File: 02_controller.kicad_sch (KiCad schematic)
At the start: 55 parts, among them J5 ISP 2x3, SW1 DIP bit 0, SW10 DIP bit 9, SW11 DIP bit 10, SW12 DIP bit 11, SW13 APPLY momentary NO, SW2 DIP bit 1, SW3 DIP bit 2, SW4 DIP bit 3, SW5 DIP bit 4, SW6 DIP bit 5, SW7 DIP bit 6, SW8 DIP bit 7, SW9 DIP bit 8, U2 1887VE7T / 4203.64-2, U6 SN74LVC125APWR, U7 SN74AHCT1G125DBVR

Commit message: Rev D schematic: ГОСТ symbols and designators in KiCad, footprints
- Three sheets regenerated by tools/dds_build.py (DDS A2, controller A3,
  power A2) with ГОСТ 2.743 symbols, ГОСТ 2.710 designators (D1.1, XW1, S2)
  and a ГОСТ 2.104 drawing sheet (lib/GOST_E3.kicad_wks).
- Connectivity identical to rev C (tools/netcompare.py with
  verification/refmap_revC_to_revD.json): 160 components, 139 nets; the 12
  single DIP switches are grouped into DIP-8 + DIP-4 packages.
- ERC: 0 errors, 0 warnings. Footprints assigned; project library lib/
  (1508PL8T LQFP-100, 1887VE7T CQFP-64 4203.64-2 preliminary, GK361-TK-02
  placeholder - not confirmed, DNP).
- Old rev C PDF replaced by output/pdf/DDS_47_51_sch.pdf.

Co-Authored-By: Claude Opus 5.5 <noreply@anthropic.com>
Claude-Session: https://claude.ai/code/session_018GorfTmWz53k1K9rRxWMAW
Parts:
- removed C39, C40, C44, C45, C46: 100n, symbol Local:C
- removed C41: 100n / U2.21, symbol Local:C
- removed C42: 100n / U2.52, symbol Local:C
- removed C43: 100n / U2.64, symbol Local:C
- removed J5: ISP 2x3, symbol Local:J6
- removed R36, R37, R38, R39, R40, R41, R42, R43, R44, R45, R46, R47, R48, R49, R50, R57, R58, R59, R60, R61, R62, R63, R64, R65: 10k, symbol Local:R
- removed R51, R52, R53, R54: 33R, symbol Local:R
- removed R55: 1k, symbol Local:R
- removed R56: 100k, symbol Local:R
- removed SW1: DIP bit 0, symbol Local:SW_SPST
- removed SW10: DIP bit 9, symbol Local:SW_SPST
- removed SW11: DIP bit 10, symbol Local:SW_SPST
- removed SW12: DIP bit 11, symbol Local:SW_SPST
- removed SW13: APPLY momentary NO, symbol Local:SW_SPST
- removed SW2: DIP bit 1, symbol Local:SW_SPST
- removed SW3: DIP bit 2, symbol Local:SW_SPST
- removed SW4: DIP bit 3, symbol Local:SW_SPST
- removed SW5: DIP bit 4, symbol Local:SW_SPST
- removed SW6: DIP bit 5, symbol Local:SW_SPST
- removed SW7: DIP bit 6, symbol Local:SW_SPST
- removed SW8: DIP bit 7, symbol Local:SW_SPST
- removed SW9: DIP bit 8, symbol Local:SW_SPST
- removed U2: 1887VE7T / 4203.64-2, symbol Local:1887VE7T
- removed U6: SN74LVC125APWR, symbol Local:LVC125
- removed U7: SN74AHCT1G125DBVR, symbol Local:AHCT1G125
- added C38, C39, C40, C41, C42, C43, C44, C45: 100n, Capacitor_SMD:C_0603_1608Metric, symbol DDS:C
- added D2: 1887ВЕ7Т, DDS:CQFP-64_4203.64-2_14x14mm_P0.8mm_1887VE7T, symbol DDS:1887VE7T
- added D3: SN74LVC125APWR, Package_SO:TSSOP-14_4.4x5mm_P0.65mm, symbol DDS:SN74LVC125A
- added D4: SN74AHCT1G125DBVR, Package_TO_SOT_SMD:SOT-23-5, symbol DDS:SN74AHCT1G125
- added R48, R49, R50, R51, R52, R53, R54, R55, R56, R57, R58, R59, R60, R61, R62, R63, R64, R65, R66, R67, R72, R73, R74, R75: 10k, Resistor_SMD:R_0603_1608Metric, symbol DDS:R
- added R68, R69, R70, R71: 33R, Resistor_SMD:R_0603_1608Metric, symbol DDS:R
- added R76: 1k, Resistor_SMD:R_0603_1608Metric, symbol DDS:R
- added R77: 100k, Resistor_SMD:R_0603_1608Metric, symbol DDS:R
- added S2: DIP-8, Button_Switch_THT:SW_DIP_SPSTx08_Slide_9.78x22.5mm_W7.62mm_P2.54mm, symbol DDS:S_DIP_x08
- added S3: DIP-4, Button_Switch_THT:SW_DIP_SPSTx04_Slide_9.78x12.34mm_W7.62mm_P2.54mm, symbol DDS:S_DIP_x04
- added S4: 6x6, Button_Switch_THT:SW_PUSH_6mm, symbol DDS:SB
- added X1: PLD-6, Connector_PinHeader_2.54mm:PinHeader_2x03_P2.54mm_Vertical, symbol DDS:X_6
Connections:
- net +3V3: now also C44.1, D3.14 (VCC), R67.1, R74.1
- net +5V: now also C41.1, C42.1, C43.1, C45.1, D2.21 (VCC), D2.52 (VCC), D2.64 (AVCC), D4.5 (VCC), R48.1, R49.1, R50.1, R51.1, R52.1, R53.1, R54.1, R55.1, R56.1, R57.1, R58.1, R59.1, R60.1, R61.1, R62.1, R65.1, X1.2
- net APPLYn: now also C38.1, D2.40 (PC5), R60.2, S4.1
- net BUF_OEn: now also D2.15 (PB5), D3.1 (EN), D3.10 (EN), D3.13 (EN), D3.4 (EN), R67.2
- net CS_BUF: now also D3.8, R70.1
- net DDS_PGOOD: now also D2.39 (PC4)
- net DDS_RSTn: now also R71.2, R75.1
- net DDS_SCK: now also R68.2, R72.1
- net DDS_SCSn: now also R70.2, R74.2
- net DDS_SDI: now also R69.2, R73.1
- net DDS_SDO: now also R76.1
- net DIP0: now also D2.51 (PA0), R48.2, S2.1
- net DIP1: now also D2.50 (PA1), R49.2, S2.2
- net DIP10: now also D2.37 (PC2), R58.2, S3.3
- net DIP11: now also D2.38 (PC3), R59.2, S3.4
- net DIP2: now also D2.49 (PA2), R50.2, S2.3
- net DIP3: now also D2.48 (PA3), R51.2, S2.4
- net DIP4: now also D2.47 (PA4), R52.2, S2.5
- net DIP5: now also D2.46 (PA5), R53.2, S2.6
- net DIP6: now also D2.45 (PA6), R54.2, S2.7
- net DIP7: now also D2.44 (PA7), R55.2, S2.8
- net DIP8: now also D2.35 (PC0), R56.2, S3.1
- net DIP9: now also D2.36 (PC1), R57.2, S3.2
- net GND: now also C38.2, C39.2, C40.2, C41.2, C42.2, C43.2, C44.2, C45.2, D2.22 (GND), D2.53 (GND), D2.63 (AGND), D3.7 (GND), D4.1 (EN), D4.3 (GND), R63.2, R64.2, R66.2, R72.2, R73.2, R75.2, R77.2, S2.10, S2.11, S2.12, S2.13, S2.14, S2.15, S2.16, S2.9, S3.5, S3.6, S3.7, S3.8, S4.2, X1.6
- net ISP_PDI: now also D2.2 (PE0), X1.4
- net ISP_PDO: now also D2.3 (PE1), X1.1
- net MCU_CS: now also D2.10 (PB0), D3.9, R65.2
- net MCU_DDS_RESET: now also D2.14 (PB4), D3.12, R66.1
- net MCU_MISO: now also D2.13 (PB3), D4.4
- net MCU_MOSI: now also D2.12 (PB2), D3.5, R64.1
- net MCU_RESETn: now also C39.1, D2.20 (RESET), R61.2, X1.5
- net MCU_SCK: now also D2.11 (PB1), D3.2, R63.1, X1.3
- net MOSI_BUF: now also D3.6, R69.1
- net RST_BUF: now also D3.11, R71.1
- net SCK_BUF: now also D3.3, R68.1
- net SDO_BUF: now also D4.2, R76.2, R77.1
- new net: D2.1 (PEN), R62.2
- new net: C40.1, D2.62 (AREF)
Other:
- note added: "D3 выключен при старте (R67); PB5 D2 — только «0» или вход"
- note added: "S2 — DIP-8 (биты 0–7), S3 — DIP-4 (биты 8–11); подтяжки R48–R59 10 кОм"
- note added: "SDO 3,3 В → 5 В через D4 (ТТЛ-входы)"
- note added: "ВКЛ (замкнут) = 1 (программная инверсия); N = 0…4000, 4001…4095 отвергаются"
- note added: "Код частоты N = Σ бит·2^i; f = 47 000 000 + 1000·N Гц"
- note added: "Согласование уровней SPI 5 В → 3,3 В"
- note removed: "02 CONTROLLER / 1887VE7T / +5 V"
- note removed: "12-bit selector / ON = 1 / N = 0..4000"
- note removed: "SPI level translation / start at 100 kHz"
- note removed: "f = 47,000,000 + 1,000*N Hz. Reject N > 4000. Debounce APPLY. Internal RC 8 MHz; ISP uses PE0/PE1. See design_notes.md for startup sequence."
- title: Controller, frequency selector and SPI -> Синтезатор частоты 47–51 МГц

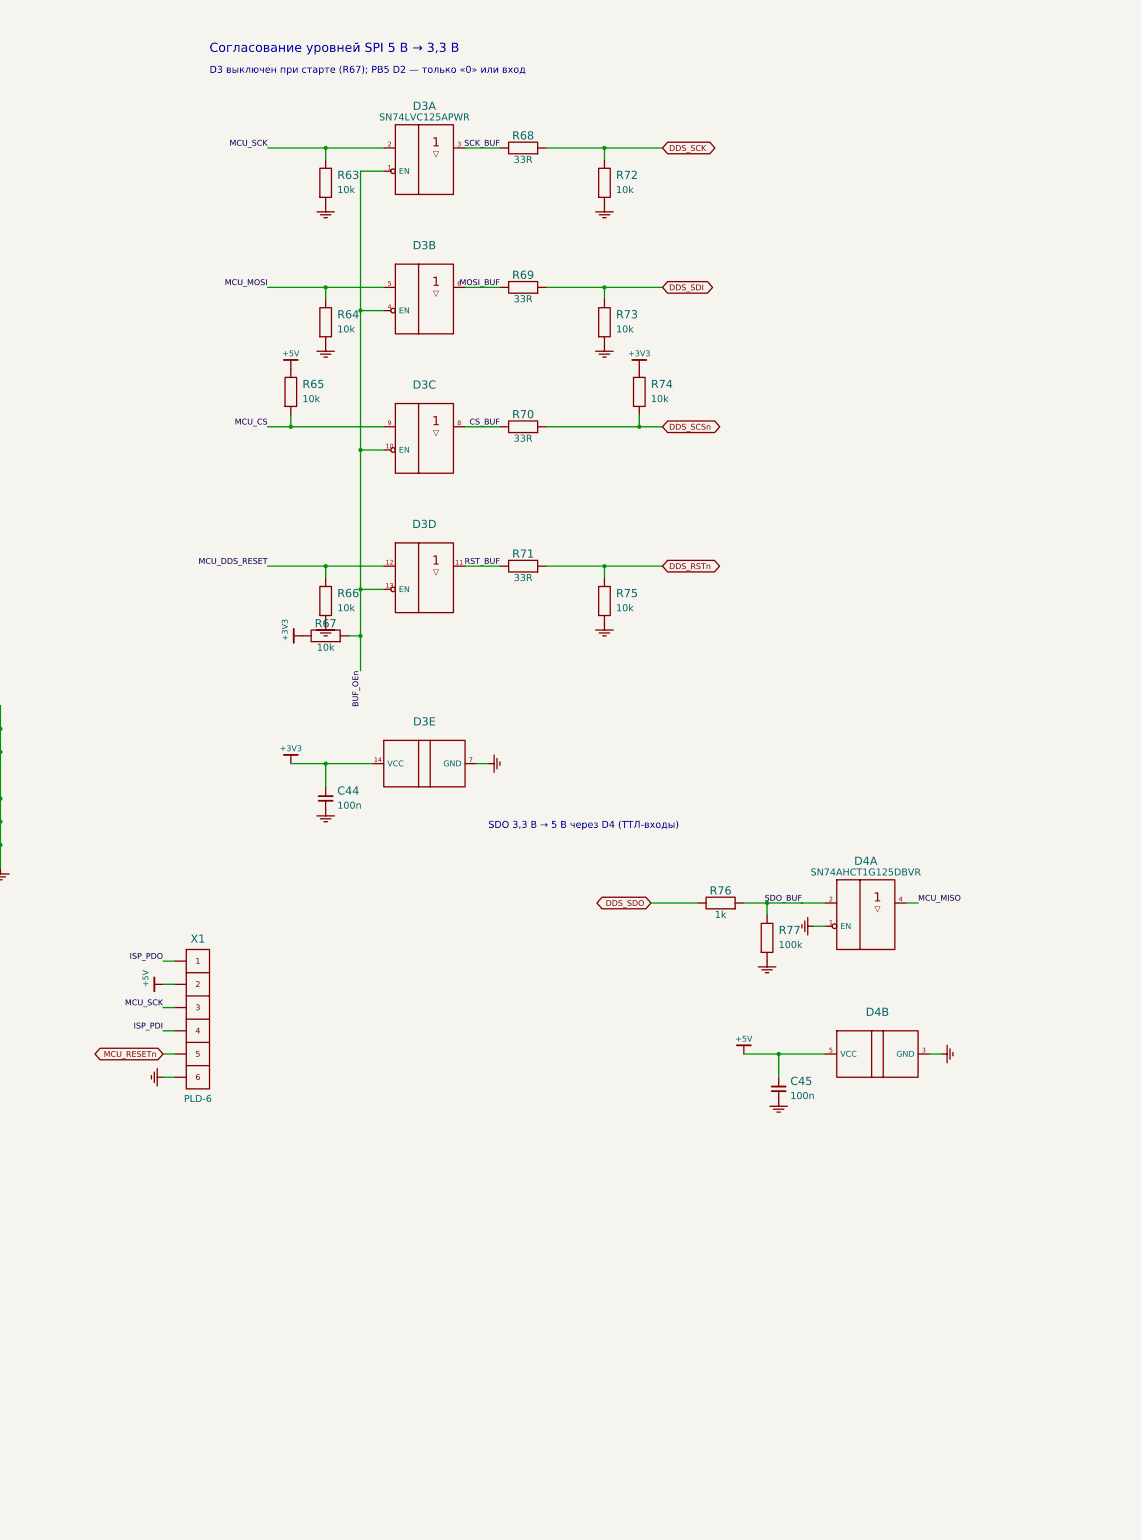
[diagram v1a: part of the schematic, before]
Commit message: Rev E: domestic regulators and logic (1393ЕУ014 + LDO, 1564АП3У2, 1594ТЛ2Т)
Power: TPS62161/2/3 replaced by a two-stage "DC/DC + LDO" scheme:
- D5 1393ЕУ014 +15 V -> +5,02 V (maker's spec v2.1 pinout; FB 40,2k/10k,
  CL 909 Ohm, soft start 100k/0,22u, EXT compensation 10k + 0,1u,
  L8 56 uH, VD2 2Д2990А, 22 uF + 100 uF tantalum output); PG -> MCU reset
- D6 1158ЕН3.3ВХ +5 V -> +3,3 V, D7 1325ЕН1.8У +5 V -> +1,8 V with a
  +5V copper heat spreader on F.Cu/B.Cu (up to 1,3 W)
- 1272ПН3Т is not used (customer decision)

SPI level shifting: SN74LVC125A -> 1564АП3У2 from +3,3 V with 1 kOhm series
resistors on all five 5 V inputs including 1OE#; SN74AHCT1G125 -> two
inverters of 1594ТЛ2Т from +5 V.

Connectivity changes in tools/eco.py; verified against the intended rev E
netlist and, for untouched parts, against rev C. ERC 0; board re-placed and
routed, DRC with schematic parity 0. Land patterns of all new domestic parts
are PLACEHOLDERS (not for fabrication). tools/pro_merge.py restores the
schematic settings that pcbnew drops from the .kicad_pro.

Co-Authored-By: Claude Opus 5.5 <noreply@anthropic.com>
Claude-Session: https://claude.ai/code/session_018GorfTmWz53k1K9rRxWMAW
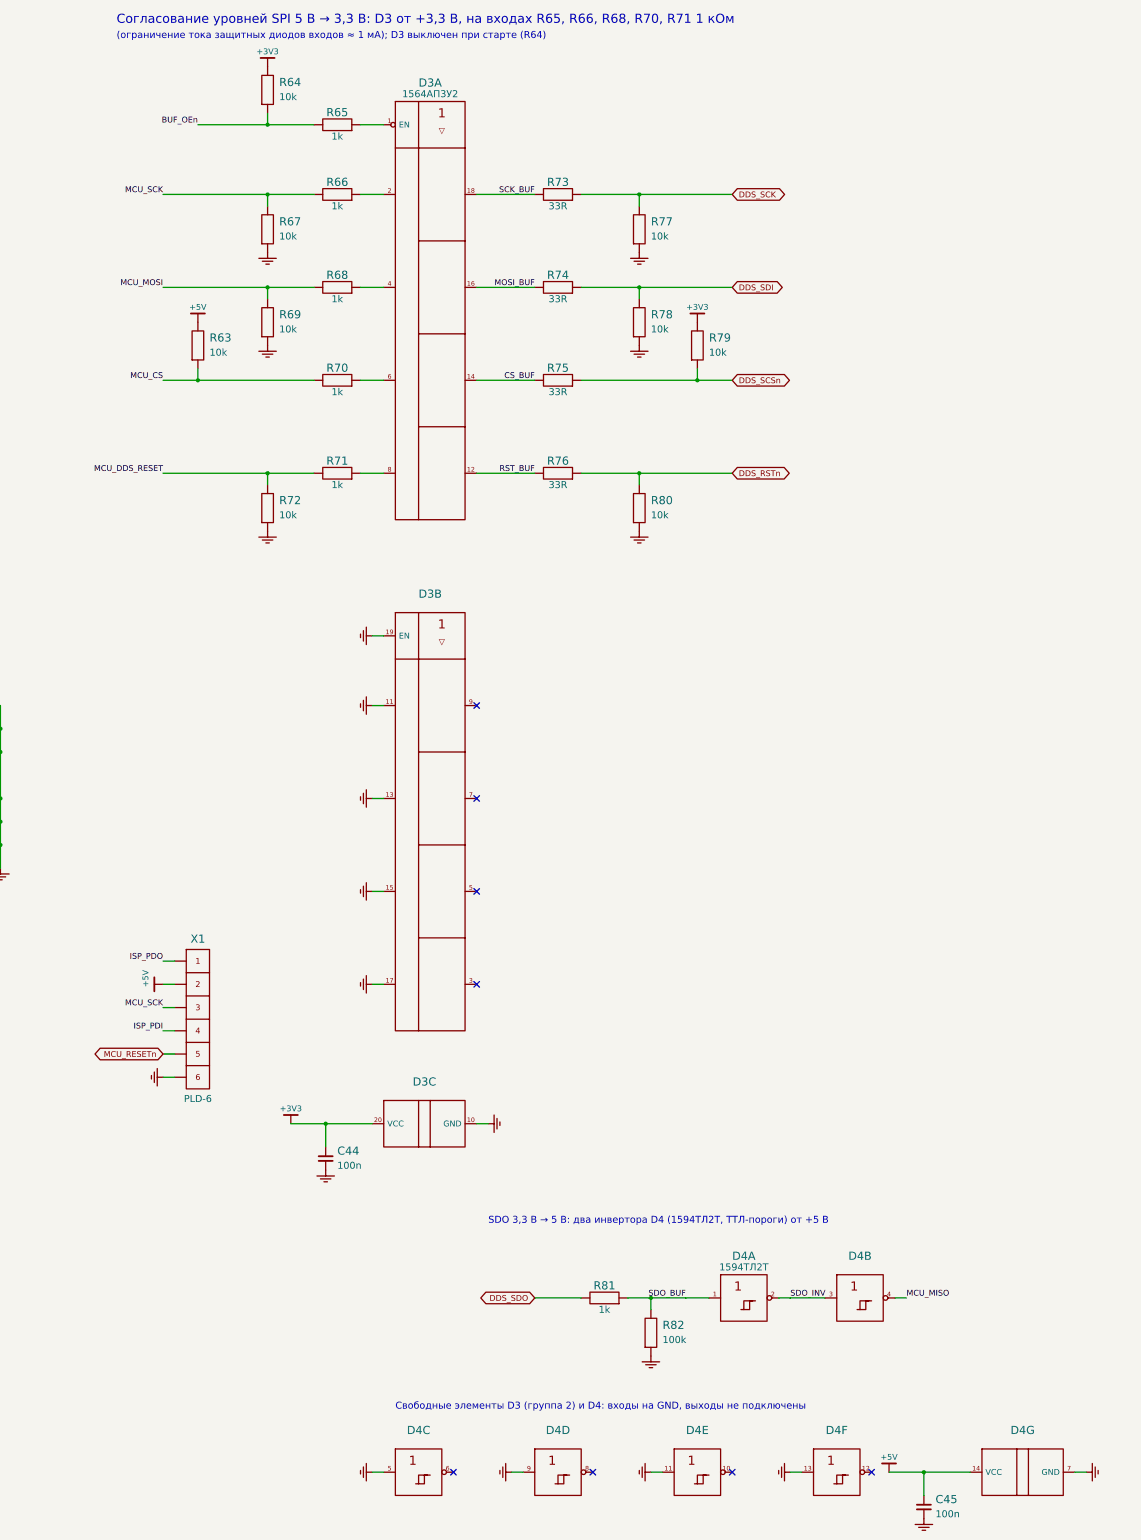
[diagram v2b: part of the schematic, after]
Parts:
- removed unit 5 of D3
- removed unit 4 of D3
- added unit 3 of D4
- added unit 6 of D4
- added unit 4 of D4
- added unit 5 of D4
- added unit 7 of D4
- added R65, R66, R68, R70, R71: 1k, Resistor_SMD:R_0603_1608Metric, symbol DDS:R
- D3: value SN74LVC125APWR -> 1564АП3У2; footprint Package_SO:TSSOP-14_4.4x5mm_P0.65mm -> DDS:SOIC-20W_1564AP3U2_PLACEHOLDER; symbol DDS:SN74LVC125A -> DDS:1564AP3; Примечание (none) -> буфер 5 -> 3,3 В, питание +3,3 В
- D4: value SN74AHCT1G125DBVR -> 1594ТЛ2Т; footprint Package_TO_SOT_SMD:SOT-23-5 -> DDS:SOIC-14_1594TL2T_PLACEHOLDER; symbol DDS:SN74AHCT1G125 -> DDS:1594TL2T; Примечание (none) -> SDO 3,3 -> 5 В, питание +5 В
- renumbered R65 to R63, R67 to R64, R63 to R67, R64 to R69, R66 to R72, R68 to R73, R69 to R74, R70 to R75, R71 to R76, R72 to R77, R73 to R78, R74 to R79, R75 to R80, R76 to R81, R77 to R82
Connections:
- net +3V3: now also D3.20 (VCC)
- net +5V: now also D4.14 (VCC); no longer D4.5 (VCC)
- net BUF_OEn: now also R65.1; no longer D3.1 (EN), D3.10 (EN), D3.4 (EN)
- net CS_BUF: now also D3.14; no longer D3.8
- net GND: now also D3.10 (GND), D3.11, D3.13, D3.15, D3.17, D3.19 (EN), D4.11, D4.13, D4.5, D4.7 (GND), D4.9; no longer D4.1 (EN), D4.3 (GND)
- net MCU_CS: now also R70.1; no longer D3.9
- net MCU_DDS_RESET: now also R71.1
- net MCU_MISO: now also D4.4; no longer D4.4
- net MCU_MOSI: now also R68.1; no longer D3.5
- net MCU_SCK: now also R66.1; no longer D3.2
- net MOSI_BUF: now also D3.16; no longer D3.6
- net RST_BUF: now also D3.12
- net SCK_BUF: now also D3.18; no longer D3.3
- net SDO_BUF: now also D4.1; no longer D4.2
- new net: D3.6, R70.2
- new net: D3.1 (EN), R65.2
- new net: D3.2, R66.2
- new net: D3.4, R68.2
- new net: D3.8, R71.2
- new net SDO_INV: D4.2, D4.3
- no-connect marks 33 -> 41
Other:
- note added: "(ограничение тока защитных диодов входов ≈ 1 мА); D3 выключен при старте (R64)"
- note added: "SDO 3,3 В → 5 В: два инвертора D4 (1594ТЛ2Т, ТТЛ-пороги) от +5 В"
- note added: "Свободные элементы D3 (группа 2) и D4: входы на GND, выходы не подключены"
- note added: "Согласование уровней SPI 5 В → 3,3 В: D3 от +3,3 В, на входах R65, R66, R68, R70, R71 1 кОм"
- note removed: "D3 выключен при старте (R67); PB5 D2 — только «0» или вход"
- note removed: "SDO 3,3 В → 5 В через D4 (ТТЛ-входы)"
- note removed: "Согласование уровней SPI 5 В → 3,3 В"
- moved on the sheet: C44, C45, D4B, R63, R64, R67, R69, R72, R73, R74, R75, R76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
